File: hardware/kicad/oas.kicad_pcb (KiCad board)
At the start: 2 copper layers, 120 x 103.5 mm, 69 parts, among them J1 Phoenix_MSTBA_2,5/3-G-5,08 (2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, J10 Native-USB recovery (DNP), J2 UART/Boot Recovery (DNP), J3 JST SM06B-GHS-TB (SEN66 conne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, J4 1x5 P1.27mm header (HLK-LD241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, J5 ESP32 row A (pins 1..15, ante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, J6 ESP32 row B (pins 16..30, USB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, J7 MIKROE mikroBUS pins 1..8 (AN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, J8 MIKROE mikroBUS pins 9..16 (P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, J9 JST SM04B-SRSS-TB (Qwiic / St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, Q1 AO3401A, SW1 C&K PTS645VK392LFS, U1 LM2596S-5.0, U2 TPS62933

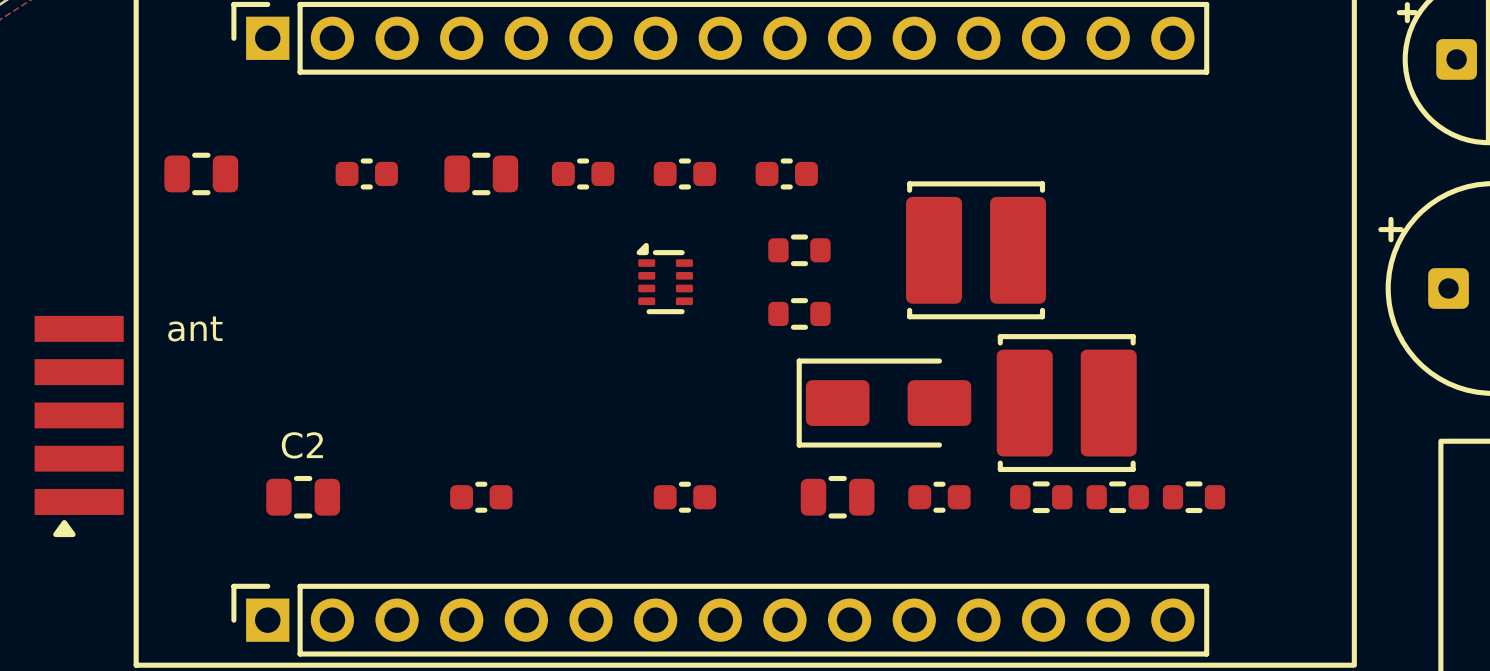
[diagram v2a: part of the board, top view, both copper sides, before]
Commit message: feat(placement): v0.50 Task-3 — re-spread buck section under ESP32
Re-place all 20 SMD power-section parts (D2 L1 U2 L2 R2 R3 C5 C6 C7 C8
C9 C13 C14 C15 C16 C17 R5 R6 R7 C2) into a clean 2-row grid inside the
user-defined rectangle (PCB-local X[-27.5,+20.5], Y[-44.5,-30] — the
gap between the ESP32 J5 and J6 pin-header rows).

- Row S (Y=-40.7): L1 C14 C5 C15 U2 C7 L2 C6 C9 C2 — power chain.
- Row N (Y=-33.5): D2 C13 C8 R2 R3 C16 C17 R5 R6 R7 — freewheel /
  BST-SS / FB divider / I2C pull-ups.
- ~5.7 mm horizontal routing corridor between the two rows; every
  courtyard now clears the J5 row (north) and J6 row (south) by
  >=3.6 mm (vs 1.26-3.04 mm in the old 3-band layout — the old south
  row tripped a JLCPCB DFM Danger).
- West->east follows the power flow: buck1 (D2/L1) west, buck2 (U2
  cluster) centre, ESP32 +3V3 decoupling + I2C pull-ups east.
- POWER_LABELS: all 20 designators on-body (dx=dy=0) on F.Fab —
  collision-free at ~3.5 mm part pitch. C2 moved F.SilkS -> F.Fab.
- Removed the ESP32 "ant" antenna-edge silk hint (not needed; the
  re-spread put L1 in that spot).

U1 / C1 / C3 / C4 / C10 out of scope, positions unchanged.
build.py 30/30 PASS, DRC 0.

Co-Authored-By: Claude Opus 4.7 (1M context) <noreply@anthropic.com>
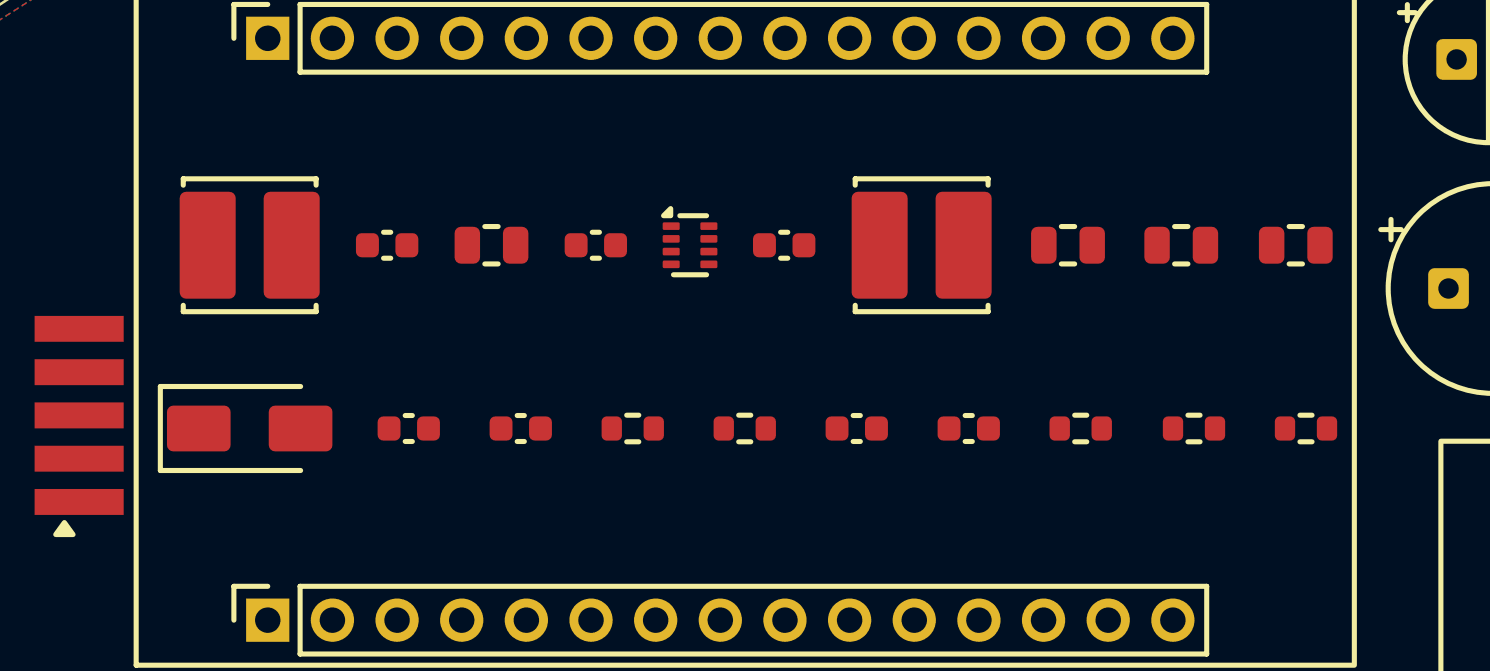
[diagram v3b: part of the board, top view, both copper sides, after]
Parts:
- moved C2 40.2 mm to (166.5, 64.3)
- moved L1 32.7 mm to (125.4, 64.3)
- moved D2 25.1 mm to (125.4, 71.5)
- moved C6 23.2 mm to (157.6, 64.3)
- moved C9 16.7 mm to (162.0, 64.3)
- moved C14 15.3 mm to (130.8, 64.3)
- moved C16 14.7 mm to (149.2, 71.5)
- moved C8 14.5 mm to (136.1, 71.5)
- moved C5 11.7 mm to (134.9, 64.3)
- moved C15 9.43 mm to (139.0, 64.3)
- moved R2 7.95 mm to (140.4, 71.5)
- moved R3 7.32 mm to (144.8, 71.5)
- moved R7 5.16 mm to (166.9, 71.5)
- moved C7 4.80 mm to (146.4, 64.3)
- moved R6 4.04 mm to (162.5, 71.5)
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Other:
- board text removed: "ant"
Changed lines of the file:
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@@
 (footprint "Diode_SMD:D_SMA"
 	(layer "F.Cu")
-	(at 150.5 70.5 0)
+	(at 125.4 71.5 0)
 (property "Reference" "D2"
 	(at 0 -2.6 0)
@@
 (footprint "Inductor_SMD:L_Cenker_CKCS5040"
 	(layer "F.Cu")
-	(at 157.5 70.5 0)
+	(at 125.4 64.3 0)
 (property "Reference" "L1"
 	(at 0 -3.6 0)
@@
 (footprint "Package_TO_SOT_SMD:SOT-583-8"
 	(layer "F.Cu")
-	(at 141.74 65.75 0)
+	(at 142.7 64.3 0)
 (property "Reference" "U2"
 	(at 0 -1.8 0)
@@
 (footprint "Inductor_SMD:L_Cenker_CKCS5040"
 	(layer "F.Cu")
-	(at 153.938 64.5 0)
+	(at 151.8 64.3 0)
 (property "Reference" "L2"
 	(at 0 -3.6 0)
@@
 (footprint "Resistor_SMD:R_0603_1608Metric"
 	(layer "F.Cu")
-	(at 147 67 0)
+	(at 140.45 71.5 0)
 (property "Reference" "R2"
 	(at 0 -1.45 0)
@@
 (footprint "Resistor_SMD:R_0603_1608Metric"
 	(layer "F.Cu")
-	(at 147 64.5 0)
+	(at 144.85 71.5 0)
 (property "Reference" "R3"
 	(at 0 -1.45 0)
@@
 (footprint "Capacitor_SMD:C_0603_1608Metric"
 	(layer "F.Cu")
-	(at 134.5 74.2 0)
+	(at 131.65 71.5 0)
 (property "Reference" "C13"
 	(at 0 -1.45 0)
@@
 (footprint "Capacitor_SMD:C_0603_1608Metric"
 	(layer "F.Cu")
-	(at 142.5 74.2 0)
+	(at 130.8 64.3 0)
 (property "Reference" "C14"
 	(at 0 -1.45 0)
@@
 (footprint "Capacitor_SMD:C_0805_2012Metric"
 	(layer "F.Cu")
-	(at 148.5 74.2 0)
+	(at 162 64.3 0)
 (property "Reference" "C9"
 	(at 0 -1.75 0)
@@
 (footprint "Capacitor_SMD:C_0603_1608Metric"
 	(layer "F.Cu")
-	(at 152.5 74.2 0)
+	(at 153.65 71.5 0)
 (property "Reference" "C17"
 	(at 0 -1.45 0)
@@
 (footprint "Resistor_SMD:R_0603_1608Metric"
 	(layer "F.Cu")
-	(at 156.5 74.2 0)
+	(at 158.05 71.5 0)
 (property "Reference" "R5"
 	(at 0 -1.45 0)
@@
 (footprint "Resistor_SMD:R_0603_1608Metric"
 	(layer "F.Cu")
-	(at 159.5 74.2 0)
+	(at 162.5 71.5 0)
 (property "Reference" "R6"
 	(at 0 -1.45 0)
@@
 (footprint "Resistor_SMD:R_0603_1608Metric"
 	(layer "F.Cu")
-	(at 162.5 74.2 0)
+	(at 166.9 71.5 0)
 (property "Reference" "R7"
 	(at 0 -1.45 0)
@@
 (footprint "Capacitor_SMD:C_0805_2012Metric"
 	(layer "F.Cu")
-	(at 123.5 61.5 0)
+	(at 134.9 64.3 0)
 (property "Reference" "C5"
 	(at 0 -1.75 0)
@@
 (footprint "Capacitor_SMD:C_0603_1608Metric"
 	(layer "F.Cu")
-	(at 130 61.5 0)
+	(at 139 64.3 0)
 (property "Reference" "C15"
 	(at 0 -1.45 0)
@@
 (footprint "Capacitor_SMD:C_0805_2012Metric"
 	(layer "F.Cu")
-	(at 134.5 61.5 0)
+	(at 157.55 64.3 0)
 (property "Reference" "C6"
 	(at 0 -1.75 0)
@@
 (footprint "Capacitor_SMD:C_0603_1608Metric"
 	(layer "F.Cu")
-	(at 138.5 61.5 0)
+	(at 149.25 71.5 0)
 (property "Reference" "C16"
 	(at 0 -1.45 0)
@@
 (footprint "Capacitor_SMD:C_0603_1608Metric"
 	(layer "F.Cu")
-	(at 142.5 61.5 0)
+	(at 146.4 64.3 0)
 (property "Reference" "C7"
 	(at 0 -1.45 0)
@@
 (footprint "Capacitor_SMD:C_0603_1608Metric"
 	(layer "F.Cu")
-	(at 146.5 61.5 0)
+	(at 136.05 71.5 0)
 (property "Reference" "C8"
 	(at 0 -1.45 0)
@@
 (footprint "Capacitor_SMD:C_0805_2012Metric"
 	(layer "F.Cu")
-	(at 127.5 74.2 0)
+	(at 166.5 64.3 0)
 (property "Reference" "C2"
 	(at 0 -1.75 0)
@@
 	(effects (font (size 1.27 1.27)))
 )
-(property "Description" "10 nF Y2 safety class — GND ↔ Earth_Protective EMI bridge. v0.43: relocated to (-21, -30.8) under the ESP32 (Y=-30.8 SMD row) — the prior spot is now occupied by J2."
+(property "Description" "10 nF Y2 safety class — GND ↔ Earth_Protective EMI bridge. v0.50 Task-3: re-placed at the east end of Row S (+18.0, -40.7)."
 	(at 0 0 0)
 	(layer "F.Fab")
@@
 	)
 )
-(gr_text "ant"
-	(at 123.24 67.6 0)
-	(layer "F.SilkS")
-	(effects
-		(font (size 1 1) (thickness 0.2))
-	)
-)
 (gr_text "USB"
 	(at 163 67.6 0)
@@
 )
 (gr_text "D2"
-	(at 150.5 67.5 0)
+	(at 125.4 71.5 0)
 	(layer "F.Fab")
 	(effects
@@
 )
 (gr_text "L1"
-	(at 157.5 66.5 0)
+	(at 125.4 64.3 0)
 	(layer "F.Fab")
 	(effects
@@
 )
 (gr_text "U2"
-	(at 141.74 63.25 0)
+	(at 142.7 64.3 0)
 	(layer "F.Fab")
 	(effects
@@
 )
 (gr_text "L2"
-	(at 153.938 60.5 0)
+	(at 151.8 64.3 0)
 	(layer "F.Fab")
 	(effects
@@
 )
 (gr_text "R2"
-	(at 147 65 0)
+	(at 140.45 71.5 0)
 	(layer "F.Fab")
 	(effects
@@
 )
 (gr_text "R3"
-	(at 147 62.5 0)
+	(at 144.85 71.5 0)
 	(layer "F.Fab")
 	(effects
@@
 )
 (gr_text "C9"
-	(at 148.5 72.2 0)
+	(at 162 64.3 0)
 	(layer "F.Fab")
 	(effects
@@
 )
 (gr_text "C13"
-	(at 134.5 72.2 0)
+	(at 131.65 71.5 0)
 	(layer "F.Fab")
 	(effects
@@
 )
 (gr_text "C14"
-	(at 142.5 72.2 0)
+	(at 130.8 64.3 0)
 	(layer "F.Fab")
 	(effects
@@
 )
 (gr_text "C17"
-	(at 152.5 72.2 0)
+	(at 153.65 71.5 0)
 	(layer "F.Fab")
 	(effects
@@
 )
 (gr_text "R5"
-	(at 156.5 72.2 0)
+	(at 158.05 71.5 0)
 	(layer "F.Fab")
 	(effects
@@
 )
 (gr_text "R6"
-	(at 159.5 72.2 0)
+	(at 162.5 71.5 0)
 	(layer "F.Fab")
 	(effects
@@
 )
 (gr_text "R7"
-	(at 162.5 72.2 0)
+	(at 166.9 71.5 0)
 	(layer "F.Fab")
 	(effects
@@
 )
 (gr_text "C5"
-	(at 126 61.5 0)
+	(at 134.9 64.3 0)
 	(layer "F.Fab")
 	(effects
@@
 )
 (gr_text "C15"
-	(at 132 61.5 0)
+	(at 139 64.3 0)
 	(layer "F.Fab")
 	(effects
@@
 )
 (gr_text "C6"
-	(at 136.5 61.5 0)
+	(at 157.55 64.3 0)
 	(layer "F.Fab")
 	(effects
@@
 )
 (gr_text "C16"
-	(at 140.5 61.5 0)
+	(at 149.25 71.5 0)
 	(layer "F.Fab")
 	(effects
@@
 )
 (gr_text "C7"
-	(at 144.5 61.5 0)
+	(at 146.4 64.3 0)
 	(layer "F.Fab")
 	(effects
@@
 )
 (gr_text "C8"
-	(at 148.5 61.5 0)
+	(at 136.05 71.5 0)
 	(layer "F.Fab")
 	(effects
@@
 )
 (gr_text "C2"
-	(at 127.5 72.2 0)
-	(layer "F.SilkS")
+	(at 166.5 64.3 0)
+	(layer "F.Fab")
 	(effects
-		(font (size 1 1) (thickness 0.2))
+		(font (size 1 1) (thickness 0.15))
 	)
 )

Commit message: fix(placement): C12 NFC decoupling — move next to J7 pin 7 (+3V3)
C12 (NT3H1101 +3V3 local decoupling) was parked ~13 mm from the NFC
power-entry pin, floating in open copper at the INT-pin Y-level. Root
cause: the placement comment counted mikroBUS pin 7 from the south end
(pre-v0.43 pin-1 location) — after the v0.43 J7/J8 180-deg flip pin 1
moved to the north end, so the real +3V3 pin (J7 pin 7) is at PCB
(-38.89, +35.56), not the +22.86 the stale comment assumed.

Re-place C12 vertical at (-31.3, +36.5) — open copper just east of
J7's +3V3/GND label pair, ~7 mm from the +3V3 pad (was ~19 mm
diagonal — too far to decouple anything).

build.py 30/30 PASS, DRC 0.

Co-Authored-By: Claude Opus 4.7 (1M context) <noreply@anthropic.com>
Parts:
- moved C12 14.9 mm to (117.2, 141.5), turned to 90 degrees
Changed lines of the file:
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@@
 (footprint "Capacitor_SMD:C_0603_1608Metric"
 	(layer "F.Cu")
-	(at 123.5 128 0)
+	(at 117.2 141.5 90)
 (property "Reference" "C12"
-	(at 0 -1.45 0)
+	(at 0 -1.45 90)
 	(layer "F.SilkS")
 			(hide yes)
@@
 )
 (property "Value" "100nF"
-	(at 0 1.45 0)
+	(at 0 1.45 90)
 	(layer "F.Fab")
 			(hide yes)
@@
 	(effects (font (size 1.27 1.27)))
 )
-(property "Description" "100 nF local decoupling for MIKROE-2462 NFC (mikroBUS pin 7 / +3V3)."
+(property "Description" "100 nF local decoupling for MIKROE-2462 NFC (mikroBUS pin 7 / +3V3). v0.50: re-placed next to J7 pin 7 (+3V3) — was ~13 mm away at the INT-pin level."
 	(at 0 0 0)
 	(layer "F.Fab")
@@
 		)
 	(pad "1" smd roundrect
-			(at -0.775 0)
+			(at -0.775 0 90)
 			(size 0.9 0.95)
 			(layers "F.Cu" "F.Mask" "F.Paste")
@@
 		)
 	(pad "2" smd roundrect
-			(at 0.775 0)
+			(at 0.775 0 90)
 			(size 0.9 0.95)
 			(layers "F.Cu" "F.Mask" "F.Paste")
@@
 )
 (gr_text "C12"
-	(at 123.5 126 0)
-	(layer "F.Fab")
-	(effects
+	(at 117.2 139.5 0)
+	(layer "F.Fab")
+	(effects

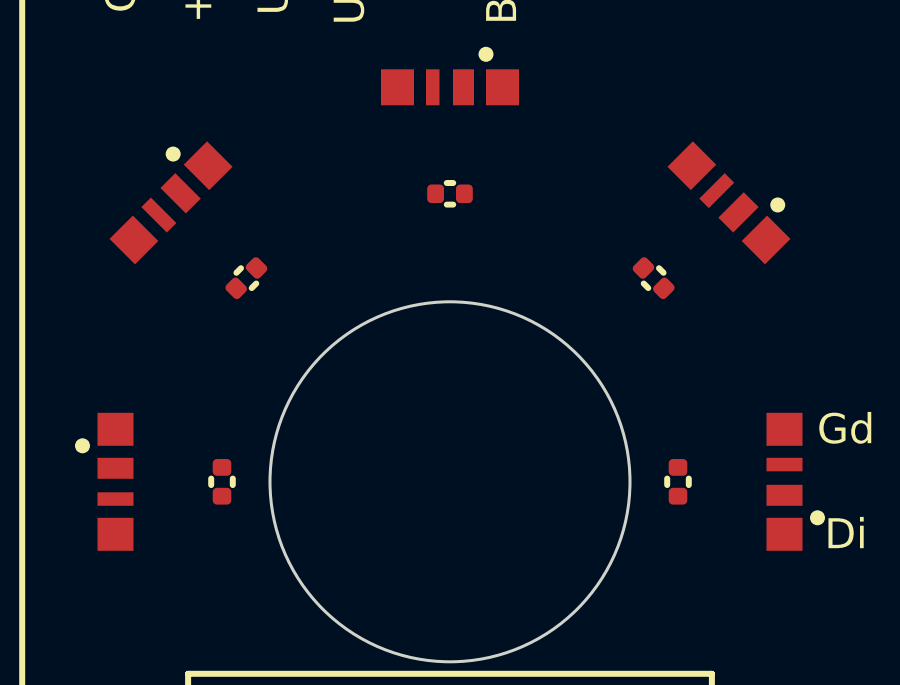
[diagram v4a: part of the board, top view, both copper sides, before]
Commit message: fix(placement): pull 5 LED-ring decoupling caps toward the centre hole
C20/C24/C25/C26/C27 re-placed at cap radius 7.0 mm (was 7.6/9.6),
vacating the annulus just inside the LED ring so the SK6812 data-chain
hops get a clear lane. Done via LED_RING_CAP_RADIAL_OFFSET_OVERRIDE:
i=0,4 offset 4.0 (LED R=11); i=5,6,7 offset 6.0 (LED R=13). Cap inner
edge ~6.66 mm, ~0.66 mm clear of the Ø12 cable hole (R=6).

C21/C23 (D12/D14 caps) deliberately excluded — they must stay outside
the J1 mating-plug no-go zone (silk rect PCB X in [-8.73,+8.73]).

Freerouting diagnostic: 87/89 -> 88/89. Net-(D16-DOUT) now closes.
Net-(D14-DOUT) still open — corridor-congestion limited (see report).

build.py 30/30 PASS, DRC 0.

Co-Authored-By: Claude Opus 4.7 (1M context) <noreply@anthropic.com>
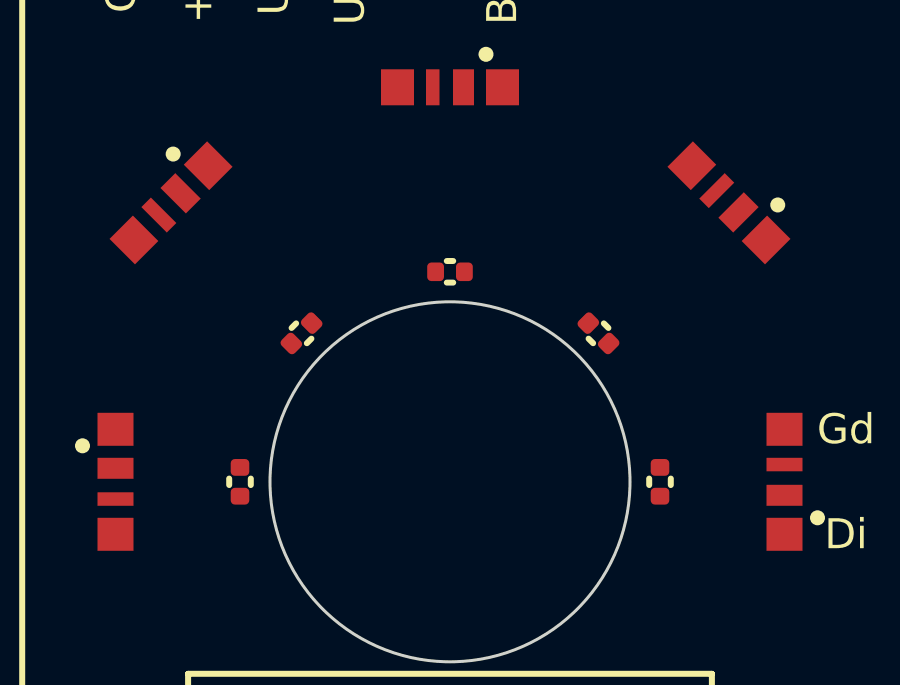
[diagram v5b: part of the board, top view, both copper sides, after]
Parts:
- moved C25 2.60 mm to (143.6, 100.1)
- moved C27 2.60 mm to (153.4, 100.1)
- moved C26 2.60 mm to (148.5, 98.0)
- moved C20 0.60 mm to (155.5, 105.0)
- moved C24 0.60 mm to (141.5, 105.0)
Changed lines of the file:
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@@
 (footprint "Capacitor_SMD:C_0402_1005Metric"
 	(layer "F.Cu")
-	(at 156.1 105 90)
+	(at 155.5 105 90)
 (property "Reference" "C20"
 	(at 0 -1.4 90)
@@
 (footprint "Capacitor_SMD:C_0402_1005Metric"
 	(layer "F.Cu")
-	(at 140.9 105 270)
+	(at 141.5 105 270)
 (property "Reference" "C24"
 	(at 0 -1.4 270)
@@
 (footprint "Capacitor_SMD:C_0402_1005Metric"
 	(layer "F.Cu")
-	(at 141.711775 98.211775 225)
+	(at 143.550253 100.050253 225)
 (property "Reference" "C25"
 	(at 0 -1.4 225)
@@
 (footprint "Capacitor_SMD:C_0402_1005Metric"
 	(layer "F.Cu")
-	(at 148.5 95.4 180)
+	(at 148.5 98 180)
 (property "Reference" "C26"
 	(at 0 -1.4 180)
@@
 (footprint "Capacitor_SMD:C_0402_1005Metric"
 	(layer "F.Cu")
-	(at 155.288225 98.211775 135)
+	(at 153.449747 100.050253 135)
 (property "Reference" "C27"
 	(at 0 -1.4 135)
